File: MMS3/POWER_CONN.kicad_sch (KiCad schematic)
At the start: 1 part, among them J7 AMASS XT60

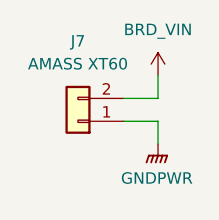
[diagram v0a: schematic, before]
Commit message: schematic + partly layout
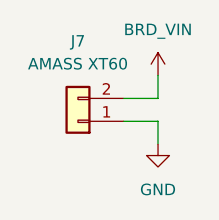
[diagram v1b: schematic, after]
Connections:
- net GNDPWR renamed GND
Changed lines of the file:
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@@
+	)
+	(symbol
+		(lib_id "power:GND")
+		(at 138.43 107.95 0)
+		(unit 1)
+		(body_style 1)
+		(exclude_from_sim no)
+		(in_bom yes)
+		(on_board yes)
+		(in_pos_files yes)
+		(dnp no)
+		(fields_autoplaced yes)
+		(property "Reference" "#PWR024"
+			(at 138.43 114.3 0)
+			(hide yes)
+			(show_name no)
+			(do_not_autoplace no)
+			(effects
+				(font
+					(size 1.27 1.27)
+				)
+			)
+		)
+		(property "Value" "GND"
+			(at 138.43 113.03 0)
+			(show_name no)
+			(do_not_autoplace no)
+			(effects
+				(font
+					(size 1.27 1.27)
+				)
+			)
+		)
+		(property "Footprint" ""
+			(at 138.43 107.95 0)
+			(hide yes)
+			(show_name no)
+			(do_not_autoplace no)
+			(effects
+				(font
+					(size 1.27 1.27)
+				)
+			)
+		)
+		(property "Datasheet" ""
+			(at 138.43 107.95 0)
+			(hide yes)
+			(show_name no)
+			(do_not_autoplace no)
+			(effects
+				(font
+					(size 1.27 1.27)
+				)
+			)
+		)
+		(property "Description" "Power symbol creates a global label with name \"GND\" , ground"
+			(at 138.43 107.95 0)
+			(hide yes)
+			(show_name no)
+			(do_not_autoplace no)
+			(effects
+				(font
+					(size 1.27 1.27)
+				)
+			)
+		)
+		(pin "1"
+		)
+		(instances
+			(project "MMS3"
+				(path "/712cea22-140d-4c92-923f-f4998caf3ecd/2a5c3dbe-0d5f-4585-982a-21b34a9f1cbf"
+					(reference "#PWR024")
+					(unit 1)
+				)
+			)
+		)
 	)
 	(symbol
@@
 					(unit 1)
 				)
-			)
-		)
-	)
-	(symbol
-		(lib_id "power:GNDPWR")
-		(at 138.43 107.95 0)
-		(unit 1)
-		(body_style 1)
-		(exclude_from_sim no)
-		(in_bom yes)
-		(on_board yes)
-		(in_pos_files yes)
-		(dnp no)
-		(fields_autoplaced yes)
-		(property "Reference" "#PWR026"
-			(at 138.43 113.03 0)
-			(hide yes)
-			(show_name no)
-			(do_not_autoplace no)
-			(effects
-				(font
-					(size 1.27 1.27)
-				)
-			)
-		)
-		(property "Value" "GNDPWR"
-			(at 138.303 111.76 0)
-			(show_name no)
-			(do_not_autoplace no)
-			(effects
-				(font
-					(size 1.27 1.27)
-				)
-			)
-		)
-		(property "Footprint" ""
-			(at 138.43 109.22 0)
-			(hide yes)
-			(show_name no)
-			(do_not_autoplace no)
-			(effects
-				(font
-					(size 1.27 1.27)
-				)
-			)
-		)
-		(property "Datasheet" ""
-			(at 138.43 109.22 0)
-			(hide yes)
-			(show_name no)
-			(do_not_autoplace no)
-			(effects
-				(font
-					(size 1.27 1.27)
-				)
-			)
-		)
-		(property "Description" "Power symbol creates a global label with name \"GNDPWR\" , global ground"
-			(at 138.43 107.95 0)
-			(hide yes)
-			(show_name no)
-			(do_not_autoplace no)
-			(effects
-				(font
-					(size 1.27 1.27)
-				)
-			)
-		)
-		(pin "1"
-		)
-		(instances
-			(project "MMS3"
-				(path "/712cea22-140d-4c92-923f-f4998caf3ecd/2a5c3dbe-0d5f-4585-982a-21b34a9f1cbf"
-					(reference "#PWR026")
-					(unit 1)
-				)
